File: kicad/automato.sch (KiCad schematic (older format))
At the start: 38 parts, among them J1 Conn_01x14_Female, J2 USB_C_Receptacle, J3 Conn_01x04_Female, J4 Conn_01x07_Male, J5 Conn_01x24_Female, Q1 Q_NPN_BCE, Q2 Q_NPN_BCE, SW1 SW_Push, SW2 SW_Push, U1 CP2102N-A01-GQFN24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

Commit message: add power indicator LED
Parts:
- added D?: LED, symbol Device:LED
- added R?: 68, symbol Device:R
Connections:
- net +3V3: now also D?.2 (A)
- net GND: now also R?.2
- new net: D?.1 (K), R?.1
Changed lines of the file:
@@
 L power:+3.3V #PWR?
 U 1 1 5FD245DA
-P 8700 2100
-F 0 "#PWR?" H 8700 1950 50  0001 C CNN
-F 1 "+3.3V" H 8715 2273 50  0000 C CNN
-F 2 "" H 8700 2100 50  0001 C CNN
-F 3 "" H 8700 2100 50  0001 C CNN
-	1    8700 2100
+P 8900 2100
+F 0 "#PWR?" H 8900 1950 50  0001 C CNN
+F 1 "+3.3V" H 8915 2273 50  0000 C CNN
+F 2 "" H 8900 2100 50  0001 C CNN
+F 3 "" H 8900 2100 50  0001 C CNN
+	1    8900 2100
 	1    0    0    -1
 $EndComp
@@
 	8200 2300 8400 2300
 Wire Wire Line
-	8700 2300 8700 2100
-Wire Wire Line
-	8400 2300 8700 2300
+	8900 2300 8900 2100
+Wire Wire Line
+	8400 2300 8900 2300
 Text GLabel 5800 2300 0    50   Input ~ 0
 VBUS
@@
 Wire Wire Line
 	5950 1550 6450 1550
+$Comp
+L Device:LED D?
+U 1 1 5FD19F97
+P 8900 2450
+F 0 "D?" V 8939 2333 50  0000 R CNN
+F 1 "LED" V 8848 2333 50  0000 R CNN
+F 2 "" H 8900 2450 50  0001 C CNN
+F 3 "~" H 8900 2450 50  0001 C CNN
+	1    8900 2450
+	0    -1   -1   0
+$EndComp
+Connection ~ 8900 2300
+$Comp
+L Device:R R?
+U 1 1 5FD1AAB8
+P 8900 2750
+F 0 "R?" H 8970 2796 50  0000 L CNN
+F 1 "68" H 8970 2705 50  0000 L CNN
+F 2 "" V 8830 2750 50  0001 C CNN
+F 3 "~" H 8900 2750 50  0001 C CNN
+	1    8900 2750
+	1    0    0    -1
+$EndComp
+$Comp
+L power:GND #PWR?
+U 1 1 5FD1B819
+P 8900 2900
+F 0 "#PWR?" H 8900 2650 50  0001 C CNN
+F 1 "GND" H 8905 2727 50  0000 C CNN
+F 2 "" H 8900 2900 50  0001 C CNN
+F 3 "" H 8900 2900 50  0001 C CNN
+	1    8900 2900
+	1    0    0    -1
+$EndComp
 $EndSCHEMATC

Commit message: add annotations
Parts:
- gave numbers to parts that had none: 10
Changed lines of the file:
@@
 ILI9341
 $Comp
-L power:+3.3V #PWR?
+L power:+3.3V #PWR033
 U 1 1 5FD245DA
 P 8900 2100
-F 0 "#PWR?" H 8900 1950 50  0001 C CNN
+F 0 "#PWR033" H 8900 1950 50  0001 C CNN
 F 1 "+3.3V" H 8915 2273 50  0000 C CNN
 F 2 "" H 8900 2100 50  0001 C CNN
@@
 $EndComp
 $Comp
-L power:GND #PWR?
+L power:GND #PWR032
 U 1 1 5FD30BBA
 P 8400 2700
-F 0 "#PWR?" H 8400 2450 50  0001 C CNN
+F 0 "#PWR032" H 8400 2450 50  0001 C CNN
 F 1 "GND" H 8405 2527 50  0000 C CNN
 F 2 "" H 8400 2700 50  0001 C CNN
@@
 $EndComp
 $Comp
-L Device:C C?
+L Device:C C4
 U 1 1 5FD4981A
 P 8400 2500
-F 0 "C?" H 8500 2500 50  0000 L CNN
+F 0 "C4" H 8500 2500 50  0000 L CNN
 F 1 "10 uF" H 8450 2400 50  0000 L CNN
 F 2 "" H 8438 2350 50  0001 C CNN
@@
 	8400 2650 8400 2700
 $Comp
-L Device:C C?
+L Device:C C3
 U 1 1 5FD6E856
 P 8200 2500
-F 0 "C?" H 8000 2500 50  0000 L CNN
+F 0 "C3" H 8000 2500 50  0000 L CNN
 F 1 "1 uF" H 8000 2400 50  0000 L CNN
 F 2 "" H 8238 2350 50  0001 C CNN
@@
 	8200 2650 8200 2700
 $Comp
-L power:GND #PWR?
+L power:GND #PWR015
 U 1 1 5FD307B3
 P 8200 2700
-F 0 "#PWR?" H 8200 2450 50  0001 C CNN
+F 0 "#PWR015" H 8200 2450 50  0001 C CNN
 F 1 "GND" H 8205 2527 50  0000 C CNN
 F 2 "" H 8200 2700 50  0001 C CNN
@@
 $EndComp
 $Comp
-L Regulator_Linear:AP2127K-3.3 U?
+L Regulator_Linear:AP2127K-3.3 U2
 U 1 1 5FCFDB8B
 P 7650 2400
-F 0 "U?" H 7650 2742 50  0000 C CNN
+F 0 "U2" H 7650 2742 50  0000 C CNN
 F 1 "AP2127K-3.3" H 7650 2651 50  0000 C CNN
 F 2 "Package_TO_SOT_SMD:SOT-23-5" H 7650 2725 50  0001 C CNN
@@
 VBUS
 $Comp
-L Device:D_Schottky D?
+L Device:D_Schottky D1
 U 1 1 5FDBB256
 P 6500 2300
-F 0 "D?" H 6500 2084 50  0000 C CNN
+F 0 "D1" H 6500 2084 50  0000 C CNN
 F 1 "MBR120" H 6500 2175 50  0000 C CNN
 F 2 "" H 6500 2300 50  0001 C CNN
@@
 	7050 2300 7350 2300
 $Comp
-L Device:R R?
+L Device:R R11
 U 1 1 5FDD496D
 P 7200 2400
-F 0 "R?" V 7300 2400 50  0000 C CNN
+F 0 "R11" V 7300 2400 50  0000 C CNN
 F 1 "100k" V 7400 2400 50  0000 C CNN
 F 2 "" V 7130 2400 50  0001 C CNN
@@
 $EndComp
 $Comp
-L power:GND #PWR?
+L power:GND #PWR014
 U 1 1 5FD0B473
 P 7650 2700
-F 0 "#PWR?" H 7650 2450 50  0001 C CNN
+F 0 "#PWR014" H 7650 2450 50  0001 C CNN
 F 1 "GND" H 7655 2527 50  0000 C CNN
 F 2 "" H 7650 2700 50  0001 C CNN
@@
 	5800 2300 6200 2300
 $Comp
-L Transistor_FET:DMP3013SFV Q?
+L Transistor_FET:DMP3013SFV Q3
 U 1 1 5FE178FD
 P 6750 1850
-F 0 "Q?" H 6956 1896 50  0000 L CNN
+F 0 "Q3" H 6956 1896 50  0000 L CNN
 F 1 "DMG3415U" H 6956 1805 50  0000 L CNN
 F 2 "Package_SON:Diodes_PowerDI3333-8" H 6950 1775 50  0001 L CIN
@@
 	6850 2300 7050 2300
 $Comp
-L Device:R R?
+L Device:R R10
 U 1 1 5FE33CDA
 P 6200 2500
-F 0 "R?" H 6270 2546 50  0000 L CNN
+F 0 "R10" H 6270 2546 50  0000 L CNN
 F 1 "100k" H 6270 2455 50  0000 L CNN
 F 2 "" V 6130 2500 50  0001 C CNN
@@
 	6200 2300 6350 2300
 $Comp
-L power:GND #PWR?
+L power:GND #PWR012
 U 1 1 5FE413C9
 P 6200 2700
-F 0 "#PWR?" H 6200 2450 50  0001 C CNN
+F 0 "#PWR012" H 6200 2450 50  0001 C CNN
 F 1 "GND" H 6205 2527 50  0000 C CNN
 F 2 "" H 6200 2700 50  0001 C CNN
@@
 	6200 1850 6200 2300
 $Comp
-L Connector:Conn_01x02_Female J?
+L Connector:Conn_01x02_Female J6
 U 1 1 5FE93309
 P 6450 1350
-F 0 "J?" V 6650 1350 50  0000 R CNN
+F 0 "J6" V 6650 1350 50  0000 R CNN
 F 1 "LiPo" V 6550 1400 50  0000 R CNN
 F 2 "" H 6450 1350 50  0001 C CNN
@@
 	6850 1550 6850 1650
 $Comp
-L power:GND #PWR?
+L power:GND #PWR011
 U 1 1 5FEBB01B
 P 5950 1700
-F 0 "#PWR?" H 5950 1450 50  0001 C CNN
+F 0 "#PWR011" H 5950 1450 50  0001 C CNN
 F 1 "GND" H 5955 1527 50  0000 C CNN
 F 2 "" H 5950 1700 50  0001 C CNN
@@
 	5950 1550 6450 1550
 $Comp
-L Device:LED D?
+L Device:LED D2
 U 1 1 5FD19F97
 P 8900 2450
-F 0 "D?" V 8939 2333 50  0000 R CNN
+F 0 "D2" V 8939 2333 50  0000 R CNN
 F 1 "LED" V 8848 2333 50  0000 R CNN
 F 2 "" H 8900 2450 50  0001 C CNN
@@
 Connection ~ 8900 2300
 $Comp
-L Device:R R?
+L Device:R R12
 U 1 1 5FD1AAB8
 P 8900 2750
-F 0 "R?" H 8970 2796 50  0000 L CNN
+F 0 "R12" H 8970 2796 50  0000 L CNN
 F 1 "68" H 8970 2705 50  0000 L CNN
 F 2 "" V 8830 2750 50  0001 C CNN
@@
 $EndComp
 $Comp
-L power:GND #PWR?
+L power:GND #PWR034
 U 1 1 5FD1B819
 P 8900 2900
-F 0 "#PWR?" H 8900 2650 50  0001 C CNN
+F 0 "#PWR034" H 8900 2650 50  0001 C CNN
 F 1 "GND" H 8905 2727 50  0000 C CNN
 F 2 "" H 8900 2900 50  0001 C CNN

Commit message: correct regulator part no: AP2112K-3.3
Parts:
- U2: value AP2127K-3.3 -> AP2112K-3.3
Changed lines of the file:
@@
 P 7650 2400
 F 0 "U2" H 7650 2742 50  0000 C CNN
-F 1 "AP2127K-3.3" H 7650 2651 50  0000 C CNN
+F 1 "AP2112K-3.3" H 7650 2651 50  0000 C CNN
 F 2 "Package_TO_SOT_SMD:SOT-23-5" H 7650 2725 50  0001 C CNN
 F 3 "https://www.diodes.com/assets/Datasheets/AP2127.pdf" H 7650 2500 50  0001 C CNN

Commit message: add (most) footprints
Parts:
- added D3: LED, symbol Device:LED
- added R13: 68, Resistor_SMD:R_0805_2012Metric, symbol Device:R
- C1, C10, C2, C3, C4, C5, C6, C7, C8, C9: footprint (none) -> Capacitor_SMD:C_0805_2012Metric
- D1: footprint (none) -> Diode_SMD:D_SOD-123F
- J2: footprint (none) -> Connector_USB:USB_C_Receptacle_Amphenol_12401610E4-2A_CircularHoles
- Q1, Q2: footprint (none) -> Package_TO_SOT_SMD:SOT-23
- R1, R10, R11, R12, R3, R4, R5, R6, R7, R8, R9: footprint (none) -> Resistor_SMD:R_0805_2012Metric
- R2: value 47.1k -> 47k; footprint (none) -> Resistor_SMD:R_0805_2012Metric
- SW1, SW2: footprint (none) -> Button_Switch_SMD:SW_Push_1P1T_NO_6x6mm_H9.5mm
- U3: footprint (none) -> RF_Module:HOPERF_RFM9XW_SMD
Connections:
- net GND: now also R13.2
- net IO26: now also D3.2 (A)
- new net: D3.1 (K), R13.1
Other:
- moved on the sheet: J5

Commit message: add SHC3 temp/humidity sensor
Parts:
- added U5: SHTC3, Sensor_Humidity:Sensirion_DFN-4-1EP_2x2mm_P1mm_EP0.7x1.6mm, symbol Sensor_Humidity:SHTC3
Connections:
- net +3V3: now also U5.1 (VDD)
- net GND: now also U5.4 (VSS)
- net I2C_SCL: now also U5.2 (SCL)
- net I2C_SDA: now also U5.3 (SDA)
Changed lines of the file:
@@
 Wire Wire Line
 	9900 6800 10200 6800
+$Comp
+L Sensor_Humidity:SHTC3 U5
+U 1 1 5FDF2FC3
+P 11450 8550
+F 0 "U5" H 11694 8596 50  0000 L CNN
+F 1 "SHTC3" H 11694 8505 50  0000 L CNN
+F 2 "Sensor_Humidity:Sensirion_DFN-4-1EP_2x2mm_P1mm_EP0.7x1.6mm" H 11650 8200 50  0001 C CNN
+F 3 "https://www.sensirion.com/fileadmin/user_upload/customers/sensirion/Dokumente/0_Datasheets/Humidity/Sensirion_Humidity_Sensors_SHTC3_Datasheet.pdf" H 11150 9000 50  0001 C CNN
+	1    11450 8550
+	1    0    0    -1
+$EndComp
+$Comp
+L power:GND #PWR037
+U 1 1 5FDF4232
+P 11550 8950
+F 0 "#PWR037" H 11550 8700 50  0001 C CNN
+F 1 "GND" H 11555 8777 50  0000 C CNN
+F 2 "" H 11550 8950 50  0001 C CNN
+F 3 "" H 11550 8950 50  0001 C CNN
+	1    11550 8950
+	1    0    0    -1
+$EndComp
+Wire Wire Line
+	11550 8850 11550 8950
+$Comp
+L power:+3.3V #PWR036
+U 1 1 5FE01F30
+P 11550 8150
+F 0 "#PWR036" H 11550 8000 50  0001 C CNN
+F 1 "+3.3V" H 11565 8323 50  0000 C CNN
+F 2 "" H 11550 8150 50  0001 C CNN
+F 3 "" H 11550 8150 50  0001 C CNN
+	1    11550 8150
+	1    0    0    -1
+$EndComp
+Wire Wire Line
+	11550 8150 11550 8250
+Text GLabel 11050 8650 0    50   Input ~ 0
+I2C_SDA
+Wire Wire Line
+	11050 8650 11150 8650
+Text GLabel 11050 8450 0    50   Input ~ 0
+I2C_SCL
+Wire Wire Line
+	11050 8450 11150 8450
 $EndSCHEMATC

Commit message: add charge controller
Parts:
- added C11: 10 uF, Capacitor_SMD:C_0805_2012Metric, symbol Device:C
- added D4: LED, symbol Device:LED
- added R14: 5.1k, Resistor_SMD:R_0805_2012Metric, symbol Device:R
- added R15: 1k, Resistor_SMD:R_0805_2012Metric, symbol Device:R
- added U6: MCP73831-2-OT, Package_TO_SOT_SMD:SOT-23-5, symbol Battery_Management:MCP73831-2-OT
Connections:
- net GND: now also C11.2, R14.2, U6.2 (VSS)
- net VBUS: now also D4.2 (A), U6.4 (VDD)
- net VBAT: now reaches J6.2 (Pin_2), Q3.5 (D)
- net VBAT: now also C11.1, U6.3 (VBAT)
- new net: R15.1, U6.1 (STAT)
- new net: R14.1, U6.5 (PROG)
- new net: D4.1 (K), R15.2
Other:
- moved on the sheet: J1, J2, J3, J5, R8, R9

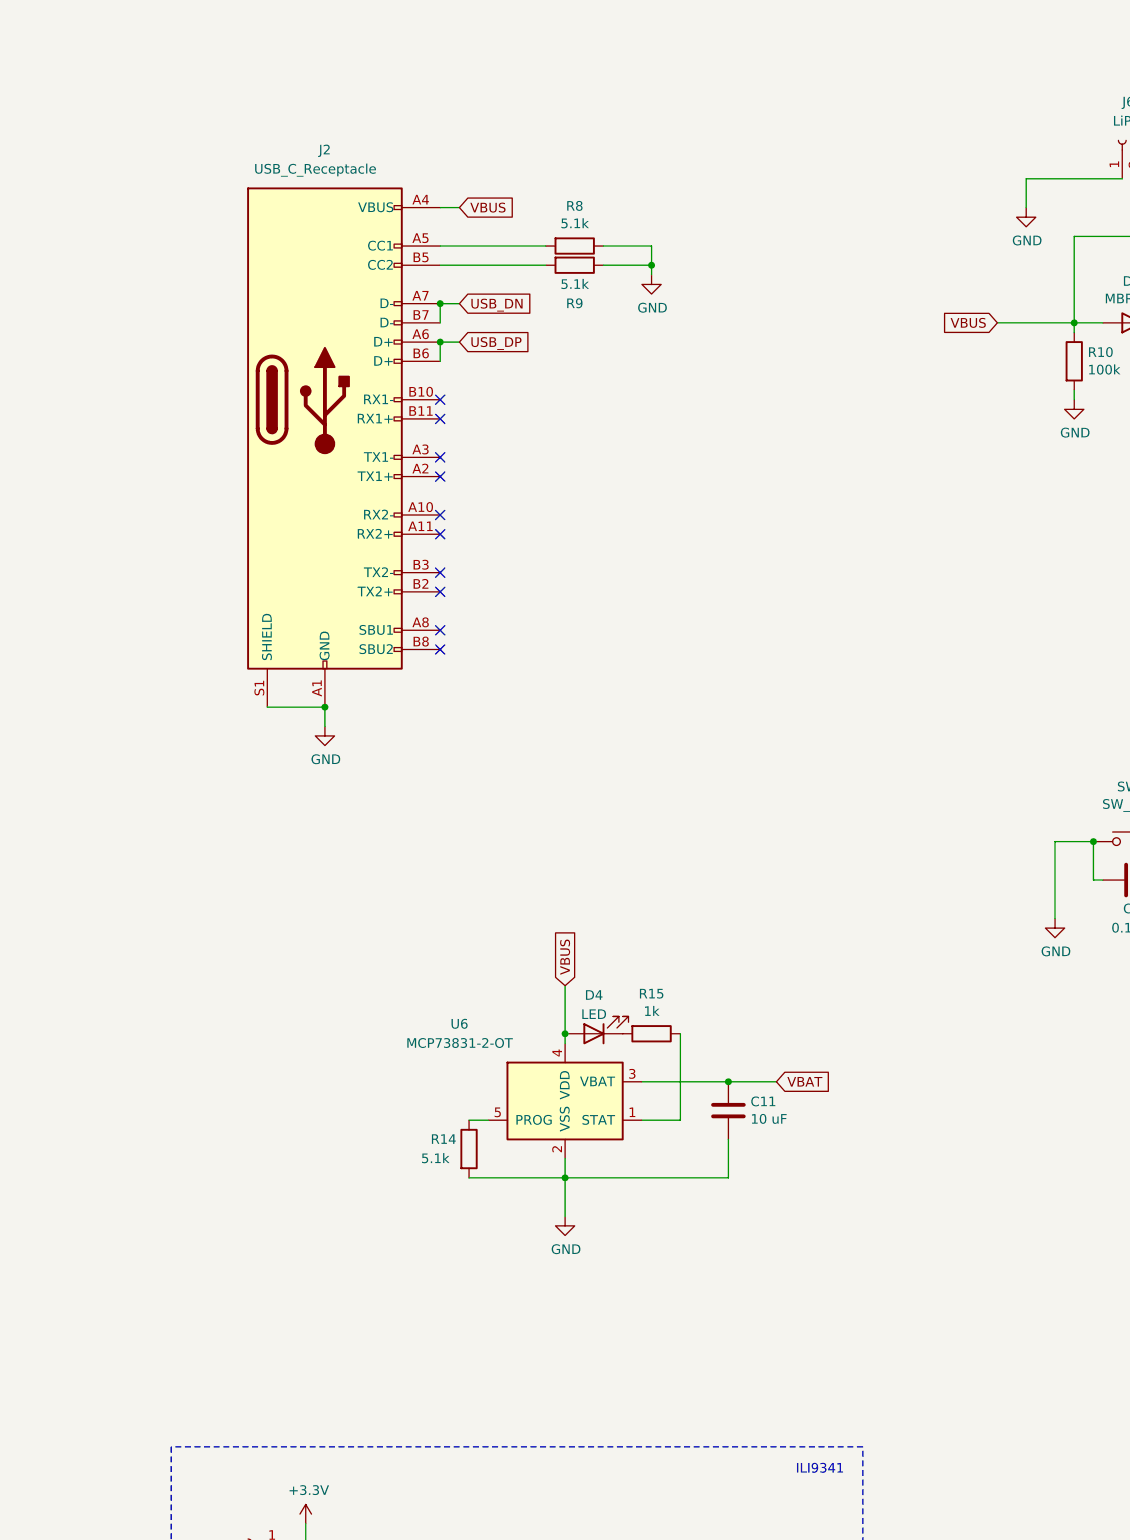
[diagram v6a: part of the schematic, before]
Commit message: Added boost and buck regulators
I still need to add some logic to enable/disable these regulators based on input voltage level/use case.  I'm guessing the easiest thing for rev1 would be to have two separate inputs for the boost and the buck?
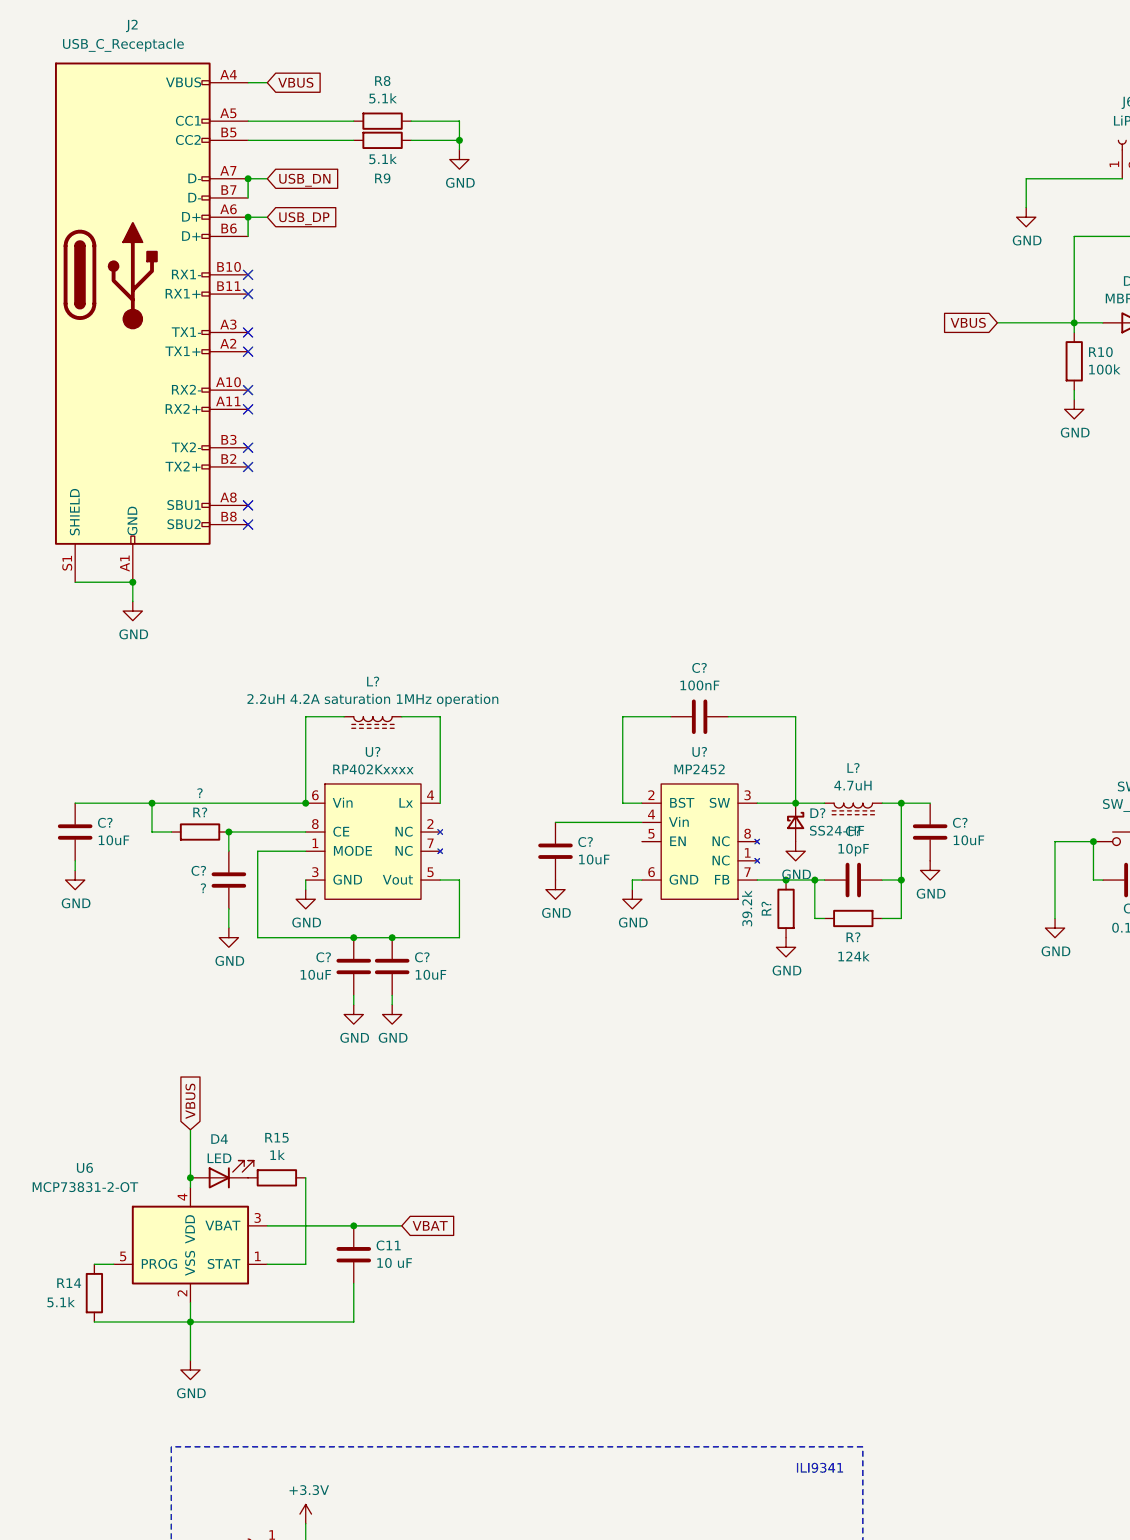
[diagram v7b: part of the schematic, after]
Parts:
- added C? (x5): 10uF, symbol Device:C
- added C?: ?, symbol Device:C
- added C?: 100nF, symbol Device:C
- added C?: 10pF, symbol Device:C
- added D?: SS24-HF, Diode_SMD:D_SMA, symbol Device:D_Schottky_Small
- added L?: 2.2uH 4.2A saturation 1MHz operation, symbol Device:L_Core_Ferrite
- added L?: 4.7uH, symbol Device:L_Core_Ferrite
- added R?: ?, Resistor_SMD:R_0805_2012Metric, symbol Device:R
- added R?: 124k, Resistor_SMD:R_0805_2012Metric, symbol Device:R
- added R?: 39.2k, Resistor_SMD:R_0805_2012Metric, symbol Device:R
- added U?: RP402Kxxxx, Package_DFN_QFN:DFN-8-1EP_2x2mm_P0.5mm_EP1.05x1.75mm, symbol automato-sensor:RP402Kxxxx
- added U?: MP2452, Package_DFN_QFN:DFN-8-1EP_3x2mm_P0.5mm_EP1.75x1.45mm, symbol automato-sensor:MP2452
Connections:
- net GND: now also C?.1, C?.1, C?.2, C?.2, C?.2, C?.2, D?.2 (A), R?.2, U?.3 (GND), U?.6 (GND)
- new net: C?.1, C?.2, U?.1 (MODE), U?.5 (Vout)
- new net: L?.1, U?.4 (Lx)
- new net: C?.1, L?.2, R?.2, U?.6 (Vin)
- new net: C?.2, R?.1, U?.8 (CE)
- new net: C?.2, U?.2 (BST)
- new net: C?.1, D?.1 (K), L?.2, U?.3 (SW)
- new net: C?.1, U?.4 (Vin)
- new net: C?.1, R?.1, R?.1, U?.7 (FB)
- new net: C?.1, C?.2, L?.1, R?.2
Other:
- moved on the sheet: C11, D4, J2, R14, R15, R8, R9, U6

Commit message: remove boost converter, connect buck via SPDT
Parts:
- removed C? (x3): 10uF, symbol Device:C
- removed C?: ?, symbol Device:C
- removed D2: LED, symbol Device:LED
- removed L?: 2.2uH 4.2A saturation 1MHz operation, symbol Device:L_Core_Ferrite
- removed R12: 68, Resistor_SMD:R_0805_2012Metric, symbol Device:R
- removed R?: ?, Resistor_SMD:R_0805_2012Metric, symbol Device:R
- removed U?: RP402Kxxxx, Package_DFN_QFN:DFN-8-1EP_2x2mm_P0.5mm_EP1.05x1.75mm, symbol automato-sensor:RP402Kxxxx
- added D5: LED, symbol Device:LED
- added R17: 1k, Resistor_SMD:R_0805_2012Metric, symbol Device:R
- added SW3: SW_SPDT, symbol Switch:SW_SPDT
- gave numbers to parts that had none: 9
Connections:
- net +3V3: now also D5.2 (A), SW3.2 (B); no longer C3.1, C4.1, U2.5 (VOUT)
- net GND: now also R17.1
- net VIN: now reaches C12.1, U7.4 (Vin)
- net at C14.2, C15.1, L1.1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: now also SW3.1 (A)
- new net: C3.1, C4.1, SW3.3 (C), U2.5 (VOUT)
- new net: D5.1 (K), R17.2
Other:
- moved on the sheet: AE1, C1, C10, C11, C12, C13, C14, C15, C2, C3, C4, C5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
